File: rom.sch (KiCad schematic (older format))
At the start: 9 parts, among them U3 23128_BASIC, U4 23128_KERNAL, U90 74LS08

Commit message: Various minor fixes
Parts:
- renumbered JP3 to JP5, JP4 to JP6, JP5 to JP7
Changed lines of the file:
@@
 singlerom_ce
 $Comp
-L Jumper:Jumper_3_Bridged12 JP3
+L Jumper:Jumper_3_Bridged12 JP5
 U 1 1 61D78514
 P 6600 3010
-F 0 "JP3" V 6646 3077 50  0000 L CNN
+F 0 "JP5" V 6646 3077 50  0000 L CNN
 F 1 "SWITCH_KCE" V 6555 3077 50  0000 L CNN
 F 2 "Jumper:SolderJumper-3_P1.3mm_Open_RoundedPad1.0x1.5mm" H 6600 3010 50  0001 C CNN
@@
 |Range      |Size      |A15|A14| Content |\n|-----------|----------|---|---|---------|\n|$0000-$3FFF|16K       | 0 | 0 | Kernal  |\n|$4000-$7FFF|16K       | 0 | 1 | Basic   |\n|$8000-$BFFF|16K       | 1 | 0 | FnLO    |\n|$C000-$FFFF|16K       | 1 | 1 | FnHI    |\n\nA15 = /CEK & /CEB\nA14 = /CEK & /CEFL\n/CEF = /CEFL & /CEFH\n/CE = /CEK & /CEB & /CEF = A15 & /CEF\n\n|/CEK|/CEB|/CEFL|/CEFH|A15|A14|/CEF|/CE|\n|----|----|-----|-----|---|---|----|---|\n|  0 |  1 |  1  |  1  | 0 | 0 |  1 | 0 |\n|  1 |  0 |  1  |  1  | 0 | 1 |  1 | 0 |\n|  1 |  1 |  0  |  1  | 1 | 0 |  0 | 0 |\n|  1 |  1 |  1  |  0  | 1 | 1 |  0 | 0 |\n|  1 |  1 |  1  |  1  | 1 | 1 |  1 | 1 |
 $Comp
-L Jumper:Jumper_3_Bridged12 JP4
+L Jumper:Jumper_3_Bridged12 JP6
 U 1 1 619F419B
 P 6600 4265
-F 0 "JP4" V 6646 4332 50  0000 L CNN
+F 0 "JP6" V 6646 4332 50  0000 L CNN
 F 1 "SWITCH_KA15" V 6555 4332 50  0000 L CNN
 F 2 "Jumper:SolderJumper-3_P1.3mm_Open_RoundedPad1.0x1.5mm" H 6600 4265 50  0001 C CNN
@@
 singlerom_a15
 $Comp
-L Jumper:Jumper_3_Bridged12 JP5
+L Jumper:Jumper_3_Bridged12 JP7
 U 1 1 61A25418
 P 6600 5540
-F 0 "JP5" V 6646 5607 50  0000 L CNN
+F 0 "JP7" V 6646 5607 50  0000 L CNN
 F 1 "SWITCH_KA14" V 6555 5607 50  0000 L CNN
 F 2 "Jumper:SolderJumper-3_P1.3mm_Open_RoundedPad1.0x1.5mm" H 6600 5540 50  0001 C CNN

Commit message: Enlarge drill holes to 0.9mm in order to make it possible to use ZIF sockets
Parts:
- U3, U4: footprint Package_DIP:DIP-28_W15.24mm_Socket_LongPads -> LittleSixteen:DIP-28_W15.24mm_Socket_LongPads
- U90: footprint Package_DIP:DIP-14_W7.62mm_Socket_LongPads -> LittleSixteen:DIP-14_W7.62mm_Socket_LongPads
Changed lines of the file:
@@
 F 0 "U3" H 3905 3155 50  0000 C CNN
 F 1 "23128_BASIC" H 3995 1060 50  0000 C CNN
-F 2 "Package_DIP:DIP-28_W15.24mm_Socket_LongPads" H 3680 2110 50  0001 C CNN
+F 2 "LittleSixteen:DIP-28_W15.24mm_Socket_LongPads" H 3680 2110 50  0001 C CNN
 F 3 "http://ww1.microchip.com/downloads/en/devicedoc/11003L.pdf" H 3680 2110 50  0001 C CNN
 	1    3680 2110
@@
 F 0 "U90" H 3860 5115 50  0000 C CNN
 F 1 "74LS08" H 3860 5024 50  0000 C CNN
-F 2 "Package_DIP:DIP-14_W7.62mm_Socket_LongPads" H 3860 4790 50  0001 C CNN
+F 2 "LittleSixteen:DIP-14_W7.62mm_Socket_LongPads" H 3860 4790 50  0001 C CNN
 F 3 "http://www.ti.com/lit/gpn/sn74LS08" H 3860 4790 50  0001 C CNN
 	1    3860 4790
@@
 F 0 "U90" H 3845 5765 50  0000 C CNN
 F 1 "74LS08" H 3845 5674 50  0000 C CNN
-F 2 "Package_DIP:DIP-14_W7.62mm_Socket_LongPads" H 3845 5440 50  0001 C CNN
+F 2 "LittleSixteen:DIP-14_W7.62mm_Socket_LongPads" H 3845 5440 50  0001 C CNN
 F 3 "http://www.ti.com/lit/gpn/sn74LS08" H 3845 5440 50  0001 C CNN
 	2    3845 5440
@@
 F 0 "U90" H 3835 6415 50  0000 C CNN
 F 1 "74LS08" H 3835 6324 50  0000 C CNN
-F 2 "Package_DIP:DIP-14_W7.62mm_Socket_LongPads" H 3835 6090 50  0001 C CNN
+F 2 "LittleSixteen:DIP-14_W7.62mm_Socket_LongPads" H 3835 6090 50  0001 C CNN
 F 3 "http://www.ti.com/lit/gpn/sn74LS08" H 3835 6090 50  0001 C CNN
 	3    3835 6090
@@
 F 0 "U90" H 3835 7060 50  0000 C CNN
 F 1 "74LS08" H 3835 6969 50  0000 C CNN
-F 2 "Package_DIP:DIP-14_W7.62mm_Socket_LongPads" H 3835 6735 50  0001 C CNN
+F 2 "LittleSixteen:DIP-14_W7.62mm_Socket_LongPads" H 3835 6735 50  0001 C CNN
 F 3 "http://www.ti.com/lit/gpn/sn74LS08" H 3835 6735 50  0001 C CNN
 	4    3835 6735
@@
 F 0 "U90" H 1400 6866 50  0000 L CNN
 F 1 "74LS08" H 1400 6775 50  0000 L CNN
-F 2 "Package_DIP:DIP-14_W7.62mm_Socket_LongPads" H 1170 6820 50  0001 C CNN
+F 2 "LittleSixteen:DIP-14_W7.62mm_Socket_LongPads" H 1170 6820 50  0001 C CNN
 F 3 "http://www.ti.com/lit/gpn/sn74LS08" H 1170 6820 50  0001 C CNN
 	5    1170 6820
@@
 F 0 "U4" H 7680 3155 50  0000 C CNN
 F 1 "23128_KERNAL" H 7770 1060 50  0000 C CNN
-F 2 "Package_DIP:DIP-28_W15.24mm_Socket_LongPads" H 7455 2110 50  0001 C CNN
+F 2 "LittleSixteen:DIP-28_W15.24mm_Socket_LongPads" H 7455 2110 50  0001 C CNN
 F 3 "http://ww1.microchip.com/downloads/en/devicedoc/11003L.pdf" H 7455 2110 50  0001 C CNN
 	1    7455 2110

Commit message: Make most ICs HCT
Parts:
- U90: value 74LS08 -> 74HCT08
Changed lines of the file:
@@
 P 3860 4790
 F 0 "U90" H 3860 5115 50  0000 C CNN
-F 1 "74LS08" H 3860 5024 50  0000 C CNN
+F 1 "74HCT08" H 3860 5024 50  0000 C CNN
 F 2 "LittleSixteen:DIP-14_W7.62mm_Socket_LongPads" H 3860 4790 50  0001 C CNN
 F 3 "http://www.ti.com/lit/gpn/sn74LS08" H 3860 4790 50  0001 C CNN
@@
 P 3845 5440
 F 0 "U90" H 3845 5765 50  0000 C CNN
-F 1 "74LS08" H 3845 5674 50  0000 C CNN
+F 1 "74HCT08" H 3845 5674 50  0000 C CNN
 F 2 "LittleSixteen:DIP-14_W7.62mm_Socket_LongPads" H 3845 5440 50  0001 C CNN
 F 3 "http://www.ti.com/lit/gpn/sn74LS08" H 3845 5440 50  0001 C CNN
@@
 P 3835 6090
 F 0 "U90" H 3835 6415 50  0000 C CNN
-F 1 "74LS08" H 3835 6324 50  0000 C CNN
+F 1 "74HCT08" H 3835 6324 50  0000 C CNN
 F 2 "LittleSixteen:DIP-14_W7.62mm_Socket_LongPads" H 3835 6090 50  0001 C CNN
 F 3 "http://www.ti.com/lit/gpn/sn74LS08" H 3835 6090 50  0001 C CNN
@@
 P 3835 6735
 F 0 "U90" H 3835 7060 50  0000 C CNN
-F 1 "74LS08" H 3835 6969 50  0000 C CNN
+F 1 "74HCT08" H 3835 6969 50  0000 C CNN
 F 2 "LittleSixteen:DIP-14_W7.62mm_Socket_LongPads" H 3835 6735 50  0001 C CNN
 F 3 "http://www.ti.com/lit/gpn/sn74LS08" H 3835 6735 50  0001 C CNN
@@
 P 1170 6820
 F 0 "U90" H 1400 6866 50  0000 L CNN
-F 1 "74LS08" H 1400 6775 50  0000 L CNN
+F 1 "74HCT08" H 1400 6775 50  0000 L CNN
 F 2 "LittleSixteen:DIP-14_W7.62mm_Socket_LongPads" H 1170 6820 50  0001 C CNN
 F 3 "http://www.ti.com/lit/gpn/sn74LS08" H 1170 6820 50  0001 C CNN

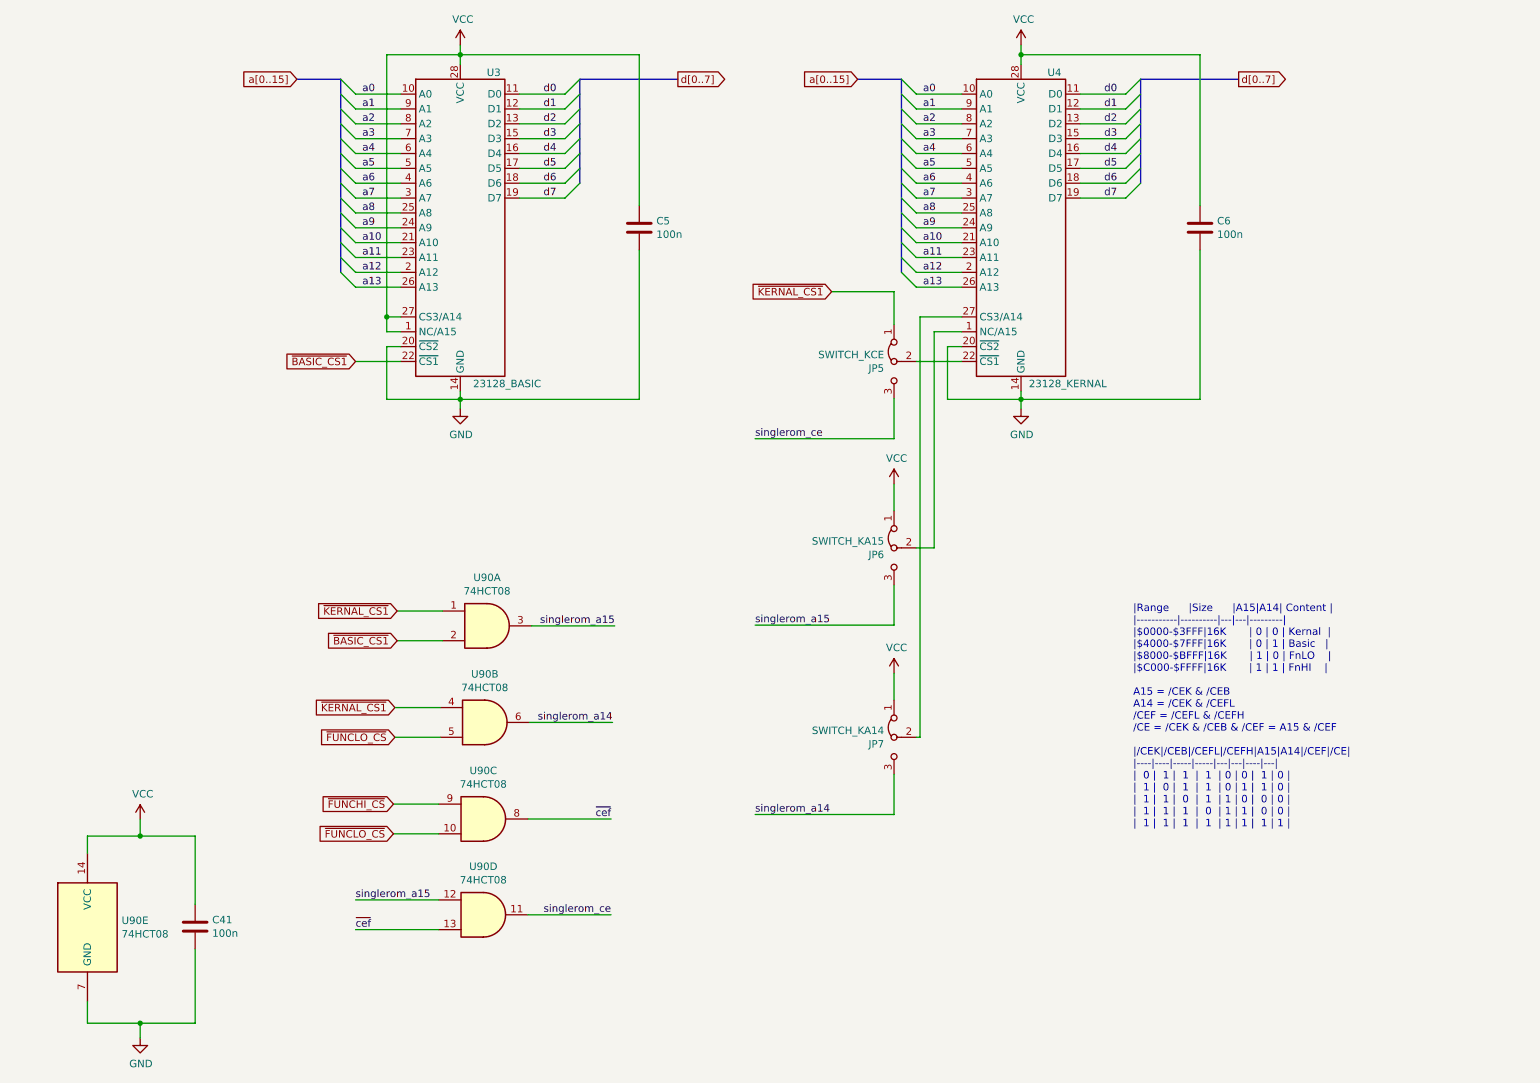
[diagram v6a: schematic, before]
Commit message: Add ROM bank switcher (All-in-one ROM only)
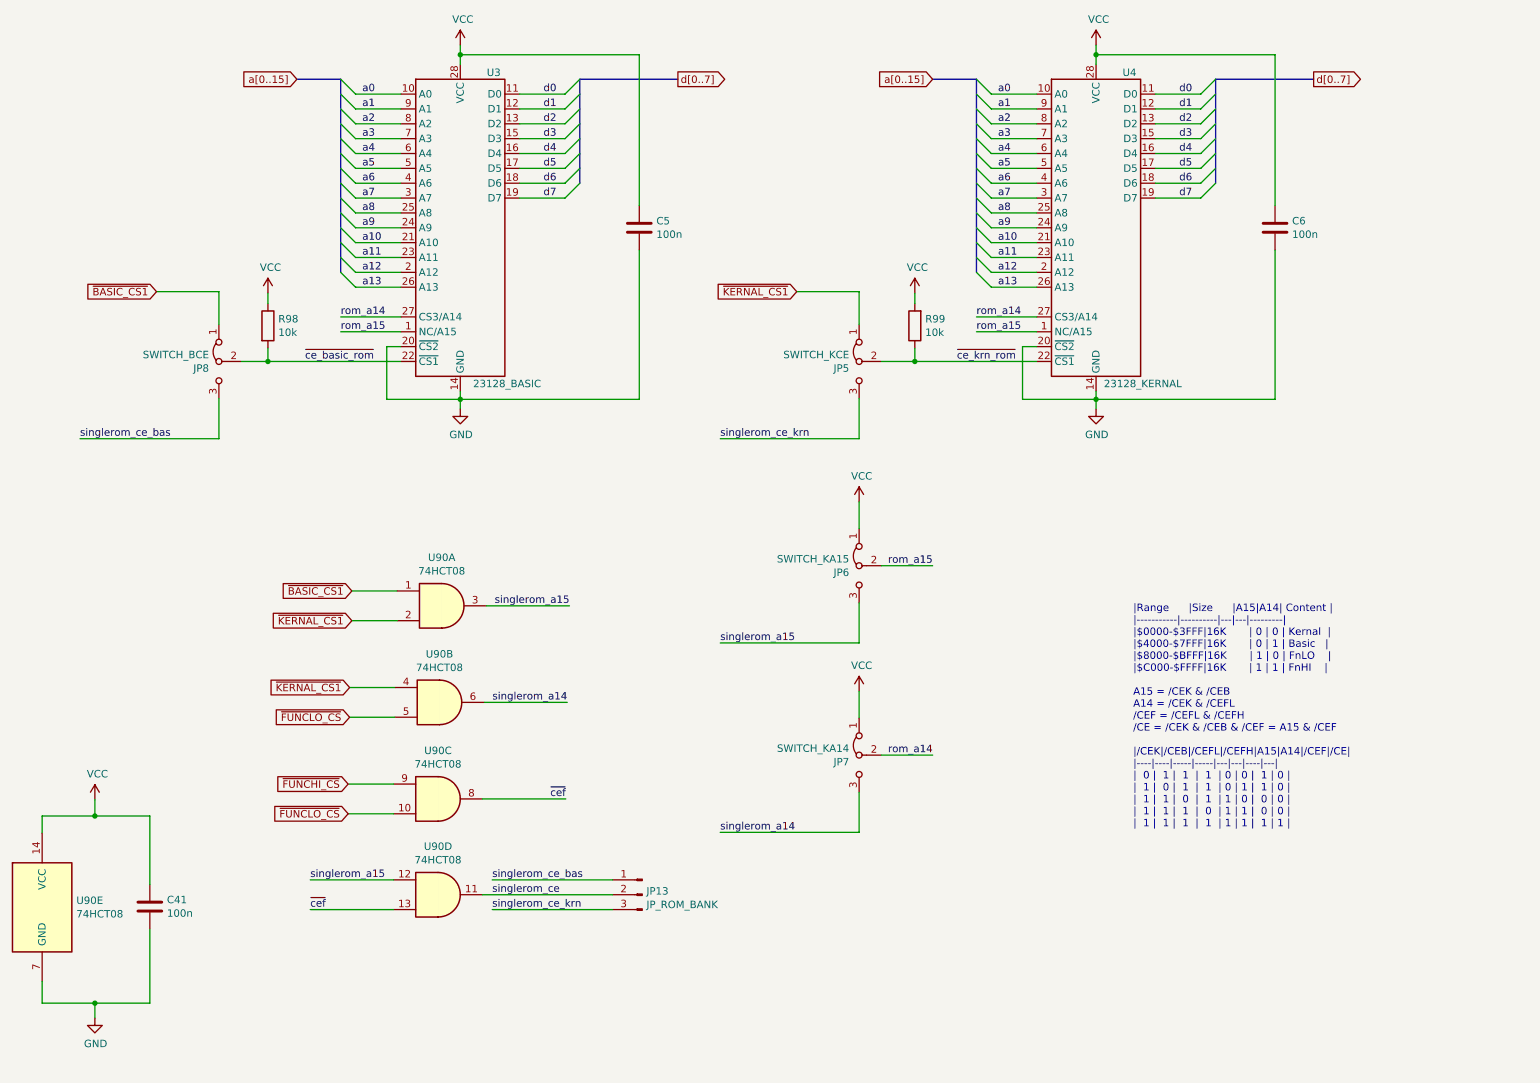
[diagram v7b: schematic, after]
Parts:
- added JP13: JP_ROM_BANK, Connector_PinHeader_2.54mm:PinHeader_1x03_P2.54mm_Vertical, symbol Connector:Conn_01x03_Male
- added JP8: SWITCH_BCE, Jumper:SolderJumper-3_P1.3mm_Open_RoundedPad1.0x1.5mm, symbol Jumper:Jumper_3_Bridged12
- added R98, R99: 10k, Resistor_THT:R_Axial_DIN0207_L6.3mm_D2.5mm_P5.08mm_Vertical, symbol Device:R
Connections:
- net VCC: now also R98.1, R99.2; no longer U3.1 (NC/A15), U3.27 (CS3/A14)
- net singlerom_ce: now also JP13.2 (Pin_2); no longer JP5.3 (B)
- net ~BASIC_CS1: now also U90.1, JP8.1 (A); no longer U3.22 (~CS1), U90.2
- net ~KERNAL_CS1: now also U90.2; no longer U90.1
- net rom_a15: now reaches JP6.2 (C), U4.1 (NC/A15)
- net rom_a15: now also U3.1 (NC/A15)
- net ~ce_krn_rom: now reaches JP5.2 (C), U4.22 (~CS1)
- net ~ce_krn_rom: now also R99.1
- net rom_a14: now reaches JP7.2 (C), U4.27 (CS3/A14)
- net rom_a14: now also U3.27 (CS3/A14)
- new net singlerom_ce_bas: JP13.1 (Pin_1), JP8.3 (B)
- new net singlerom_ce_krn: JP13.3 (Pin_3), JP5.3 (B)
- new net ~ce_basic_rom: JP8.2 (C), R98.2, U3.22 (~CS1)
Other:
- moved on the sheet: C41, C6, JP5, U4, U90A, U90B, U90C, U90D, U90E
